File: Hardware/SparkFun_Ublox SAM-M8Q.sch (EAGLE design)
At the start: 34 parts, among them J13 Qwiic Right Angle, J4 Qwiic Right Angle, U2 UBLOX_SAM-M8Q

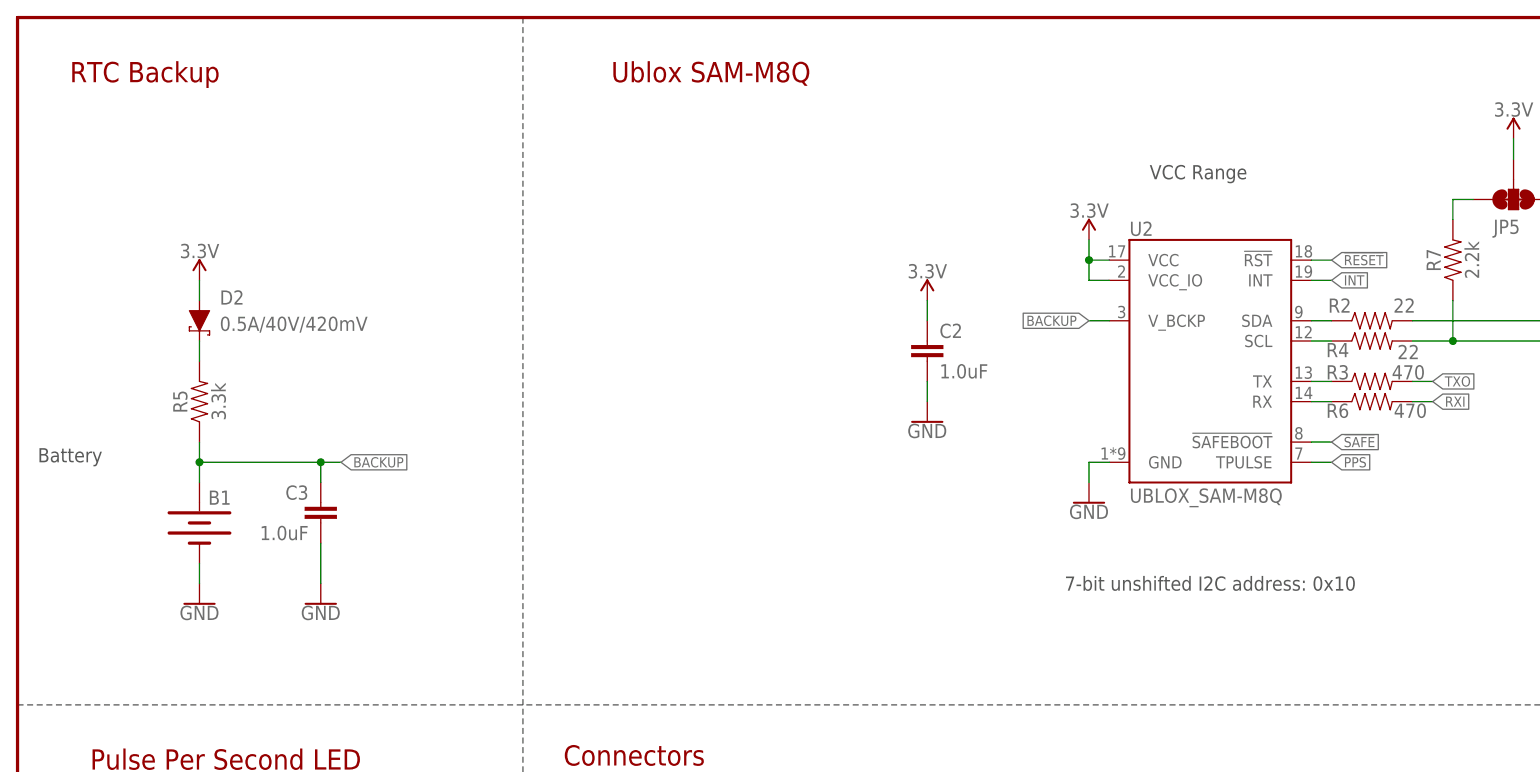
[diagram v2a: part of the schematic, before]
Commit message: Updates GPS module with updated part, adds VCC range and Battery text to schematic
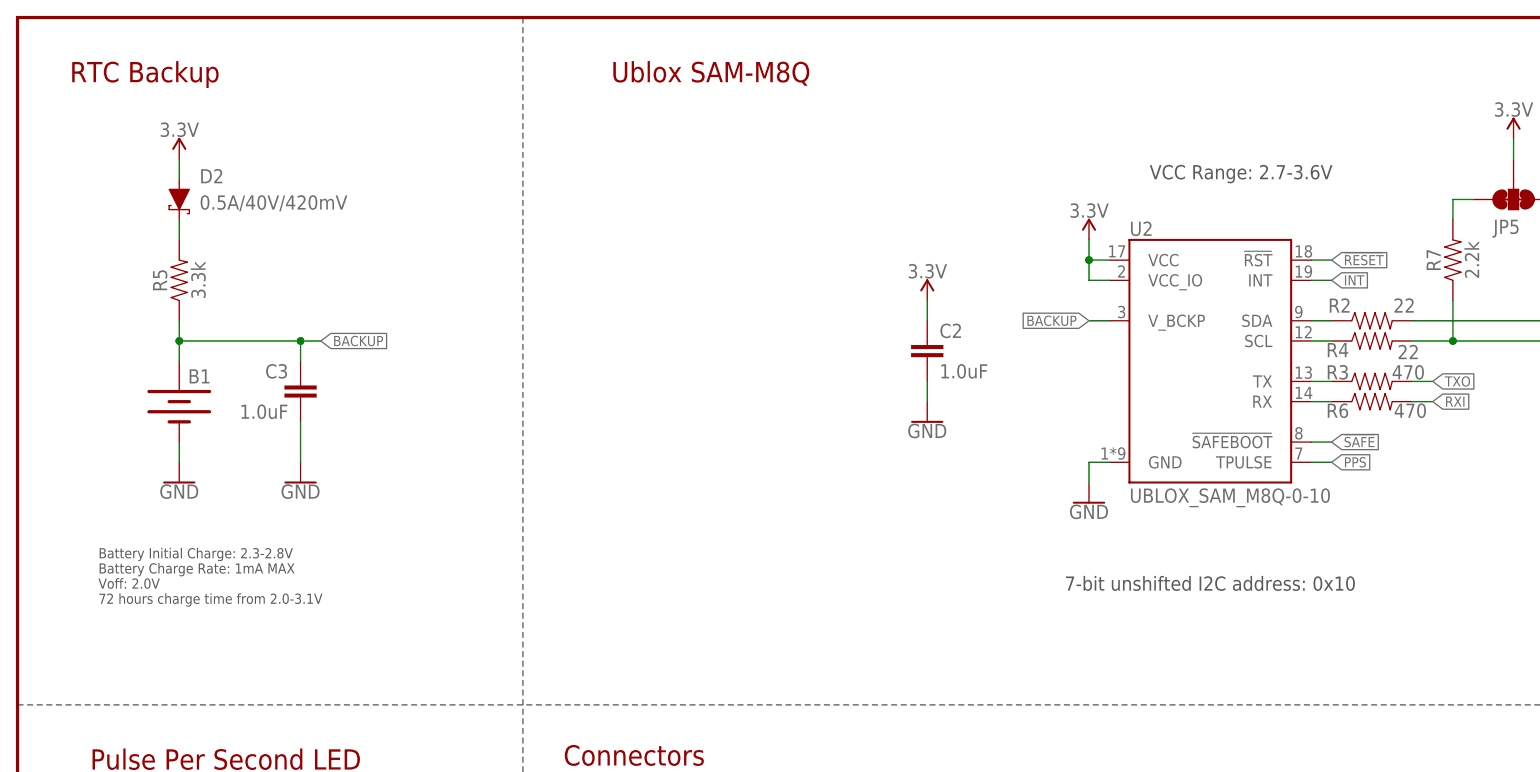
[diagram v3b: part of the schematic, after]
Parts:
- U2: value UBLOX_SAM-M8Q -> UBLOX_SAM_M8Q-0-10; device SparkFun-GPS:UBLOX_SAM-M8Q -> SparkFun-GPS:UBLOX_SAM_M8Q-0-10
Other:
- note added: "Battery Initial Charge: 2.3-2.8V Battery Charge Rate: 1mA MAX Voff: 2.0V 72 hours charge time from 2.0-3.1V"
- note added: "VCC Range: 2.7-3.6V"
- note removed: "Battery"
- note removed: "VCC Range"
- moved on the sheet: B1, C3, D2, R5
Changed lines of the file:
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@@
 <?xml version="1.0" encoding="utf-8"?>
 <!DOCTYPE eagle SYSTEM "eagle.dtd">
-<eagle version="9.3.0">
+<eagle version="9.2.1">
 <drawing>
 <settings>
@@
 <part name="JP7" library="SparkFun-Aesthetics" deviceset="FIDUCIAL" device="UFIDUCIAL"/>
 <part name="JP8" library="SparkFun-Aesthetics" deviceset="FIDUCIAL" device="UFIDUCIAL"/>
-<part name="U2" library="SparkFun-GPS" deviceset="UBLOX_SAM-M8Q" device=""/>
+<part name="U2" library="SparkFun-GPS" deviceset="UBLOX_SAM_M8Q-0-10" device=""/>
 <part name="R2" library="SparkFun-Resistors" deviceset="22OHM" device="-0603-1/10W-1%" value="22"/>
 <part name="R4" library="SparkFun-Resistors" deviceset="22OHM" device="-0603-1/10W-1%" value="22"/>
@@
 disable Power
 LED</text>
-<text x="142.24" y="165.1" size="1.778" layer="97" font="vector" ratio="12">VCC Range</text>
-<text x="2.54" y="129.54" size="1.778" layer="97" font="vector" ratio="12">Battery</text>
+<text x="142.24" y="165.1" size="1.778" layer="97" font="vector" ratio="12">VCC Range: 2.7-3.6V</text>
+<text x="10.16" y="111.76" size="1.27" layer="97" font="vector">Battery Initial Charge: 2.3-2.8V
+Battery Charge Rate: 1mA MAX
+Voff: 2.0V
+72 hours charge time from 2.0-3.1V</text>
 </plain>
 <instances>
@@
 <attribute name="VALUE" x="175.006" y="135.128" size="1.778" layer="96" font="vector" rot="R180" align="top-center"/>
 </instance>
-<instance part="C3" gate="G$1" x="38.1" y="121.92" smashed="yes" rot="MR0">
-<attribute name="NAME" x="36.576" y="124.841" size="1.778" layer="95" font="vector" rot="MR0"/>
-<attribute name="VALUE" x="36.576" y="119.761" size="1.778" layer="96" font="vector" rot="MR0"/>
-</instance>
-<instance part="B1" gate="G$1" x="22.86" y="121.92" smashed="yes" rot="R270">
-<attribute name="NAME" x="25.4" y="124.206" size="1.778" layer="95" font="vector" rot="MR0" align="bottom-center"/>
-</instance>
-<instance part="GND5" gate="1" x="22.86" y="111.76" smashed="yes">
-<attribute name="VALUE" x="22.86" y="111.506" size="1.778" layer="96" font="vector" align="top-center"/>
-</instance>
-<instance part="GND10" gate="1" x="38.1" y="111.76" smashed="yes">
-<attribute name="VALUE" x="38.1" y="111.506" size="1.778" layer="96" font="vector" align="top-center"/>
+<instance part="C3" gate="G$1" x="35.56" y="137.16" smashed="yes" rot="MR0">
+<attribute name="NAME" x="34.036" y="140.081" size="1.778" layer="95" font="vector" rot="MR0"/>
+<attribute name="VALUE" x="34.036" y="135.001" size="1.778" layer="96" font="vector" rot="MR0"/>
+</instance>
+<instance part="B1" gate="G$1" x="20.32" y="137.16" smashed="yes" rot="R270">
+<attribute name="NAME" x="22.86" y="139.446" size="1.778" layer="95" font="vector" rot="MR0" align="bottom-center"/>
+</instance>
+<instance part="GND5" gate="1" x="20.32" y="127" smashed="yes">
+<attribute name="VALUE" x="20.32" y="126.746" size="1.778" layer="96" font="vector" align="top-center"/>
+</instance>
+<instance part="GND10" gate="1" x="35.56" y="127" smashed="yes">
+<attribute name="VALUE" x="35.56" y="126.746" size="1.778" layer="96" font="vector" align="top-center"/>
 </instance>
 <instance part="SUPPLY6" gate="G$1" x="114.3" y="149.86" smashed="yes" rot="MR0">
@@
 <attribute name="VALUE" x="12.7" y="60.96" size="1.778" layer="96" font="vector" align="top-left"/>
 </instance>
-<instance part="D2" gate="G$1" x="22.86" y="147.32" smashed="yes" rot="R270">
-<attribute name="NAME" x="25.4" y="149.352" size="1.778" layer="95" font="vector"/>
-<attribute name="VALUE" x="25.4" y="147.828" size="1.778" layer="96" font="vector" align="top-left"/>
-</instance>
-<instance part="SUPPLY5" gate="G$1" x="22.86" y="152.4" smashed="yes">
-<attribute name="VALUE" x="22.86" y="155.194" size="1.778" layer="96" font="vector" align="bottom-center"/>
-</instance>
-<instance part="R5" gate="G$1" x="22.86" y="137.16" smashed="yes" rot="R90">
-<attribute name="NAME" x="21.336" y="137.16" size="1.778" layer="95" font="vector" rot="R90" align="bottom-center"/>
-<attribute name="VALUE" x="24.384" y="137.16" size="1.778" layer="96" font="vector" rot="R90" align="top-center"/>
+<instance part="D2" gate="G$1" x="20.32" y="162.56" smashed="yes" rot="R270">
+<attribute name="NAME" x="22.86" y="164.592" size="1.778" layer="95" font="vector"/>
+<attribute name="VALUE" x="22.86" y="163.068" size="1.778" layer="96" font="vector" align="top-left"/>
+</instance>
+<instance part="SUPPLY5" gate="G$1" x="20.32" y="167.64" smashed="yes">
+<attribute name="VALUE" x="20.32" y="170.434" size="1.778" layer="96" font="vector" align="bottom-center"/>
+</instance>
+<instance part="R5" gate="G$1" x="20.32" y="152.4" smashed="yes" rot="R90">
+<attribute name="NAME" x="18.796" y="152.4" size="1.778" layer="95" font="vector" rot="R90" align="bottom-center"/>
+<attribute name="VALUE" x="21.844" y="152.4" size="1.778" layer="96" font="vector" rot="R90" align="top-center"/>
 </instance>
 <instance part="R11" gate="G$1" x="7.62" y="55.88" smashed="yes" rot="R90">
@@
 <pinref part="D2" gate="G$1" pin="A"/>
 <pinref part="SUPPLY5" gate="G$1" pin="3.3V"/>
-<wire x1="22.86" y1="152.4" x2="22.86" y2="149.86" width="0.1524" layer="91"/>
+<wire x1="20.32" y1="167.64" x2="20.32" y2="165.1" width="0.1524" layer="91"/>
 </segment>
 <segment>
@@
 <segment>
 <pinref part="C3" gate="G$1" pin="2"/>
-<wire x1="38.1" y1="119.38" x2="38.1" y2="114.3" width="0.1524" layer="91"/>
+<wire x1="35.56" y1="134.62" x2="35.56" y2="129.54" width="0.1524" layer="91"/>
 <pinref part="GND10" gate="1" pin="GND"/>
 </segment>
 <segment>
 <pinref part="B1" gate="G$1" pin="-"/>
-<wire x1="22.86" y1="116.84" x2="22.86" y2="114.3" width="0.1524" layer="91"/>
+<wire x1="20.32" y1="132.08" x2="20.32" y2="129.54" width="0.1524" layer="91"/>
 <pinref part="GND5" gate="1" pin="GND"/>
 </segment>
@@
 <segment>
 <pinref part="C3" gate="G$1" pin="1"/>
-<wire x1="38.1" y1="129.54" x2="38.1" y2="127" width="0.1524" layer="91"/>
+<wire x1="35.56" y1="144.78" x2="35.56" y2="142.24" width="0.1524" layer="91"/>
 <pinref part="B1" gate="G$1" pin="+"/>
-<wire x1="38.1" y1="129.54" x2="22.86" y2="129.54" width="0.1524" layer="91"/>
-<wire x1="22.86" y1="129.54" x2="22.86" y2="127" width="0.1524" layer="91"/>
-<wire x1="38.1" y1="129.54" x2="40.64" y2="129.54" width="0.1524" layer="91"/>
-<junction x="38.1" y="129.54"/>
-<label x="40.64" y="129.54" size="1.27" layer="95" font="vector" xref="yes"/>
+<wire x1="35.56" y1="144.78" x2="20.32" y2="144.78" width="0.1524" layer="91"/>
+<wire x1="20.32" y1="144.78" x2="20.32" y2="142.24" width="0.1524" layer="91"/>
+<wire x1="35.56" y1="144.78" x2="38.1" y2="144.78" width="0.1524" layer="91"/>
+<junction x="35.56" y="144.78"/>
+<label x="38.1" y="144.78" size="1.27" layer="95" font="vector" xref="yes"/>
 <pinref part="R5" gate="G$1" pin="1"/>
-<wire x1="22.86" y1="132.08" x2="22.86" y2="129.54" width="0.1524" layer="91"/>
-<junction x="22.86" y="129.54"/>
+<wire x1="20.32" y1="147.32" x2="20.32" y2="144.78" width="0.1524" layer="91"/>
+<junction x="20.32" y="144.78"/>
 </segment>
 <segment>
@@
 <pinref part="D2" gate="G$1" pin="C"/>
 <pinref part="R5" gate="G$1" pin="2"/>
-<wire x1="22.86" y1="144.78" x2="22.86" y2="142.24" width="0.1524" layer="91"/>
-</segment>
-</net>
+<wire x1="20.32" y1="160.02" x2="20.32" y2="157.48" width="0.1524" layer="91"/>
+</segment>
+</net>
